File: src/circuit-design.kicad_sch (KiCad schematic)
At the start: 32 parts, among them J1 USB_C_Receptacle_USB2.0_16P, J2 Conn_01x08_Pin, J3 Conn_01x08_Pin, SW1 SW_Push, SW2 SW_Push, U1 USBLC6-2SC6, U2 AP2112K-3.3, U3 ESP32-C3-WROOM-02, Y1 Crystal

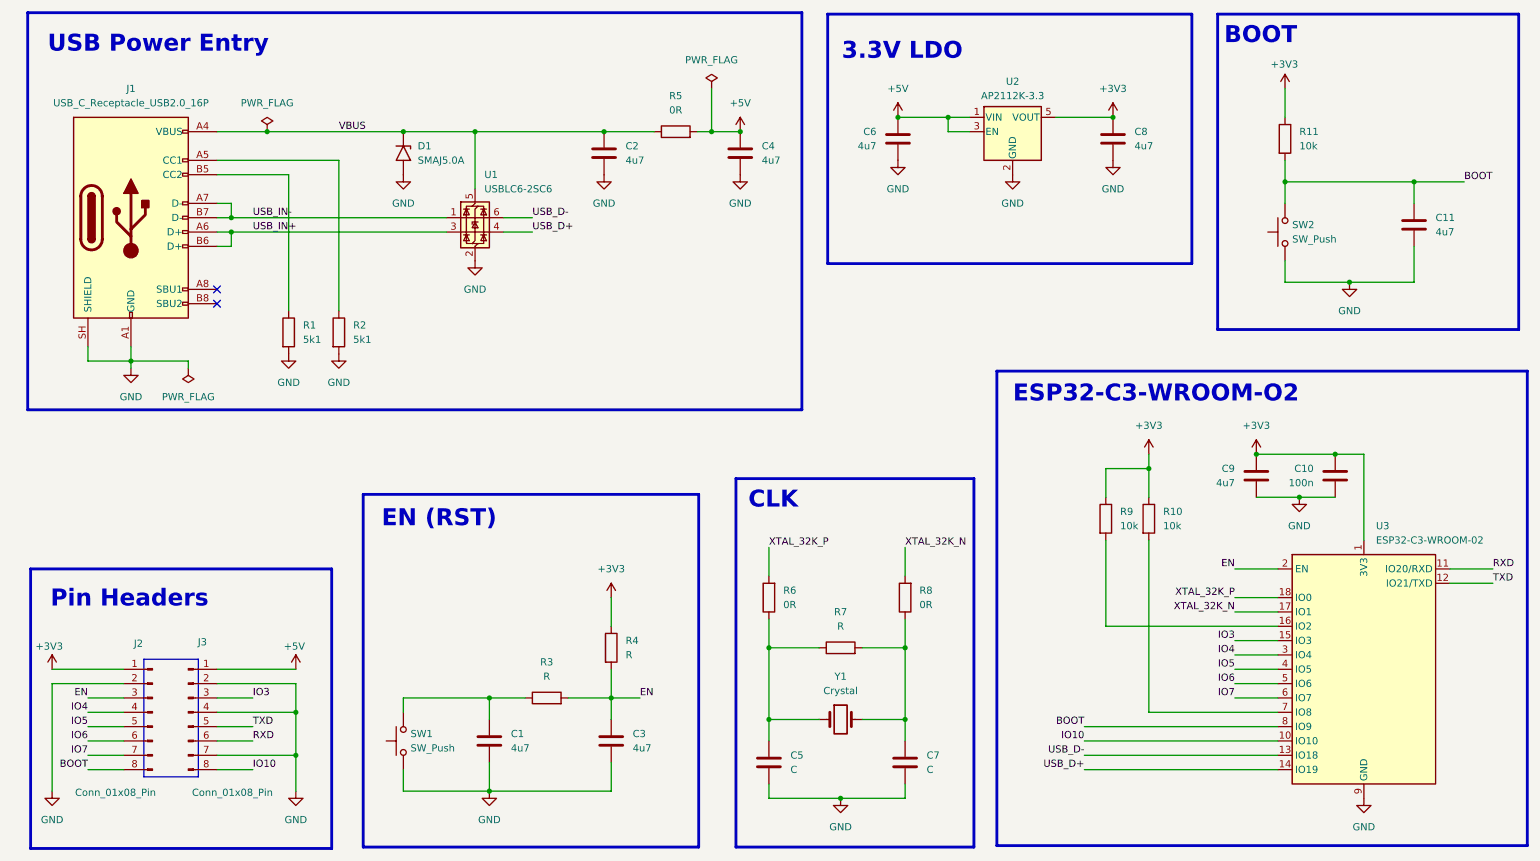
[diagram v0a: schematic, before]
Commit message: refactor(sch/usb): replace circuit protection devices symbols with own database symbols
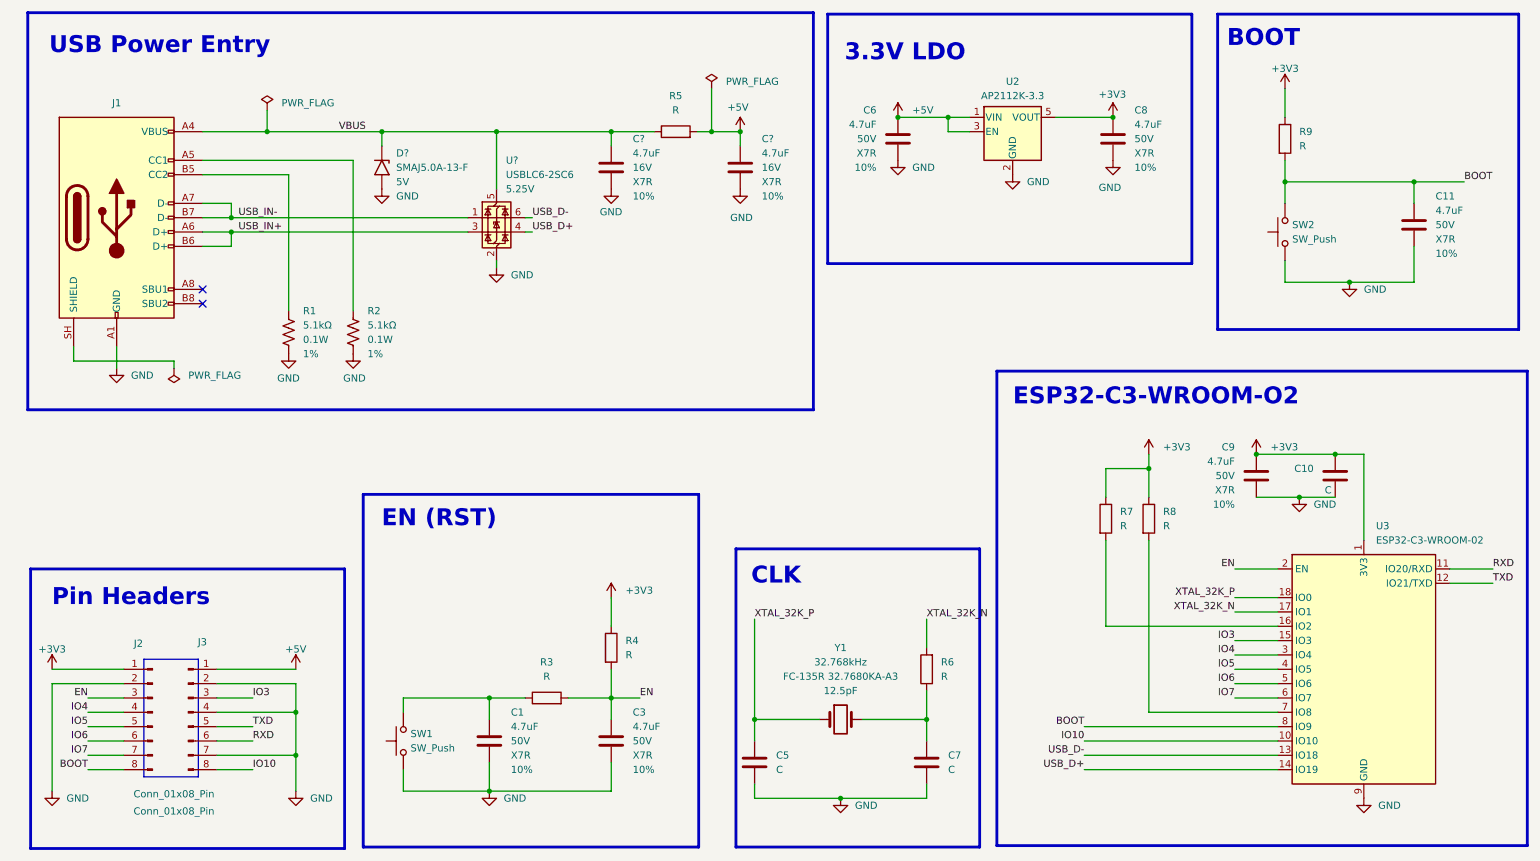
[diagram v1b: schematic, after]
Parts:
- removed C2, C4, C6, C9: 4u7, Capacitor_SMD:C_0603_1608Metric, symbol Device:C
- removed D1: SMAJ5.0A, Diode_SMD:D_SMA, symbol Diode:SMAJ5.0A
- removed R6, R8: 0R, Resistor_SMD:R_0603_1608Metric, symbol Device:R
- removed U1: USBLC6-2SC6, Package_TO_SOT_SMD:SOT-23-6, symbol Power_Protection:USBLC6-2SC6
- removed Y1: Crystal, Crystal:Crystal_SMD_3215-2Pin_3.2x1.5mm, symbol Device:Crystal
- added C6, C9: 4.7uF, #LZ_Capacitor_SMD:C_0603_1608Metric, symbol #lzg:cap/CAP-0009-0475
- added C? (x2): 4.7uF, #LZ_Capacitor_SMD:C_0603_1608Metric, symbol #lz:cap/CAP-0009-0475
- added D?: SMAJ5.0A-13-F, Diode_SMD:D_SMA, symbol #lz:cpd/CPD-0001-5V00
- added U?: USBLC6-2SC6, Package_TO_SOT_SMD:SOT-23-6, symbol #lz:cpd/CPD-0002-5V25
- added Y1: 32.768kHz, Crystal:Crystal_SMD_3215-2Pin_3.2x1.5mm, symbol #lzg:xtl/XTL-0001-32K7
- C1, C11, C3, C8: value 4u7 -> 4.7uF; footprint Capacitor_SMD:C_0603_1608Metric -> #LZ_Capacitor_SMD:C_0603_1608Metric; symbol Device:C -> #lzg:cap/CAP-0009-0475; Capacitance (none) -> 4.7uF; IPN (none) -> CAP-0009-0475; MPN GRM188Z71A475KE15D -> GRM188Z71C475KE21D; Manufacturer (none) -> Murata; Material (none) -> X7R; Tolerance (none) -> 10%; Voltage (none) -> 50V
- C10: value 100n -> C; footprint Capacitor_SMD:C_0603_1608Metric -> (none); MPN GRM188R71H104KA93D -> (none)
- C5, C7: footprint Capacitor_SMD:C_0603_1608Metric -> (none)
- J1: value USB_C_Receptacle_USB2.0_16P -> USB-C 16P; footprint Connector_USB:USB_C_Receptacle_G-Switch_GT-USB-7010ASV -> Connector_USB:USB_C_Receptacle_GCT_USB4105-xx-A_16P_TopMnt_Horizontal; symbol Connector:USB_C_Receptacle_USB2.0_16P -> #lz:con/CON-0001-0016; IPN (none) -> CON-0001-0016; MPN (none) -> USB4105-GF-A-120; Manufacturer (none) -> Global Connector Technology; Positions (none) -> 16
- J2, J3: footprint Connector_PinHeader_2.54mm:PinHeader_1x08_P2.54mm_Vertical -> (none)
- R1, R2: value 5k1 -> 5.1kΩ; footprint Resistor_SMD:R_0603_1608Metric -> #LZ_Resistor_SMD:R_0603_1608Metric; symbol Device:R -> #lz:res/RES-0001-5101; IPN (none) -> RES-0001-5101; MPN (none) -> RC0603FR-075K1L; Manufacturer (none) -> Yageo; Package (none) -> 0603; Power (none) -> 0.1W; Resistance (none) -> 5.1kΩ; Tolerance (none) -> 1%
- R3, R4: footprint Resistor_SMD:R_0603_1608Metric -> (none)
- R5: value 0R -> R; footprint Resistor_SMD:R_0603_1608Metric -> (none)
- R6: renamed from R7; footprint Resistor_SMD:R_0603_1608Metric -> (none)
- R7: renamed from R9; value 10k -> R; footprint Resistor_SMD:R_0603_1608Metric -> (none)
- R8: renamed from R10; value 10k -> R; footprint Resistor_SMD:R_0603_1608Metric -> (none)
- R9: renamed from R11; value 10k -> R; footprint Resistor_SMD:R_0603_1608Metric -> (none)
- SW1, SW2: footprint Button_Switch_SMD:SW_SPST_B3U-1000P -> (none); MPN B3U-1000P -> (none)
- U2: MPN AP2112K-3.3 -> (none)
- U3: MPN ESP32-C3-WROOM-02-N4 -> (none)
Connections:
- net +3V3: now also C9.1
- net +5V: now also C6.1, C?.1
- net GND: now also C6.2, C9.2, C?.2, C?.2, D?.2 (A2), U?.2 (GND); no longer J1.SH (SHIELD)
- net USB_D+: now also U?.4 (I/O2)
- net USB_D-: now also U?.6 (I/O1)
- net USB_IN+: now also U?.3 (I/O2)
- net USB_IN-: now also U?.1 (I/O1)
- net VBUS: now also C?.1, D?.1 (A1), U?.5 (VBUS)
- net XTAL_32K_N: now also R6.2
- net XTAL_32K_P: now also C5.1, Y1.1
- net at C7.1: now also R6.1, Y1.2; no longer R6.2
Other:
- moved on the sheet: C5, C7, J1, R6

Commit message: feat(sch): add MPN for RPUs and R filter
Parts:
- removed R3, R4, R5, R7, R8, R9: R, symbol Device:R
- added R3, R4, R7, R8, R9: 10kΩ, #LZ_Resistor_SMD:R_0603_1608Metric, symbol #lz:res/RES-0001-1002
- added R5: 1Ω, #LZ_Resistor_SMD:R_0603_1608Metric, symbol #lz:res/RES-0001-1R00
- C1, C11, C3, C6, C8, C9: symbol #lzg:cap/CAP-0009-0475 -> #lz:cap/CAP-0009-0475; Voltage 50V -> 16V
- Y1: symbol #lzg:xtl/XTL-0001-32K7 -> #lz:xtl/XTL-0001-32K7
- gave numbers to parts that had none: 4
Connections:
- net +3V3: now also R4.1, R7.1, R8.1, R9.1
- net +5V: now also R5.2
- net BOOT: now also R9.2
- net EN: now also R3.2, R4.2
- net GND: now also J1.SH (SHIELD)
- net VBUS: now also R5.1
- net at U3.16 (IO2): now also R7.2
- net at U3.7 (IO8): now also R8.2
- net at C1.1, SW1.2: now also R3.1
